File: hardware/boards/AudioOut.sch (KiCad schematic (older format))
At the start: 9 parts, among them J4 AudioJack3_SwitchTR

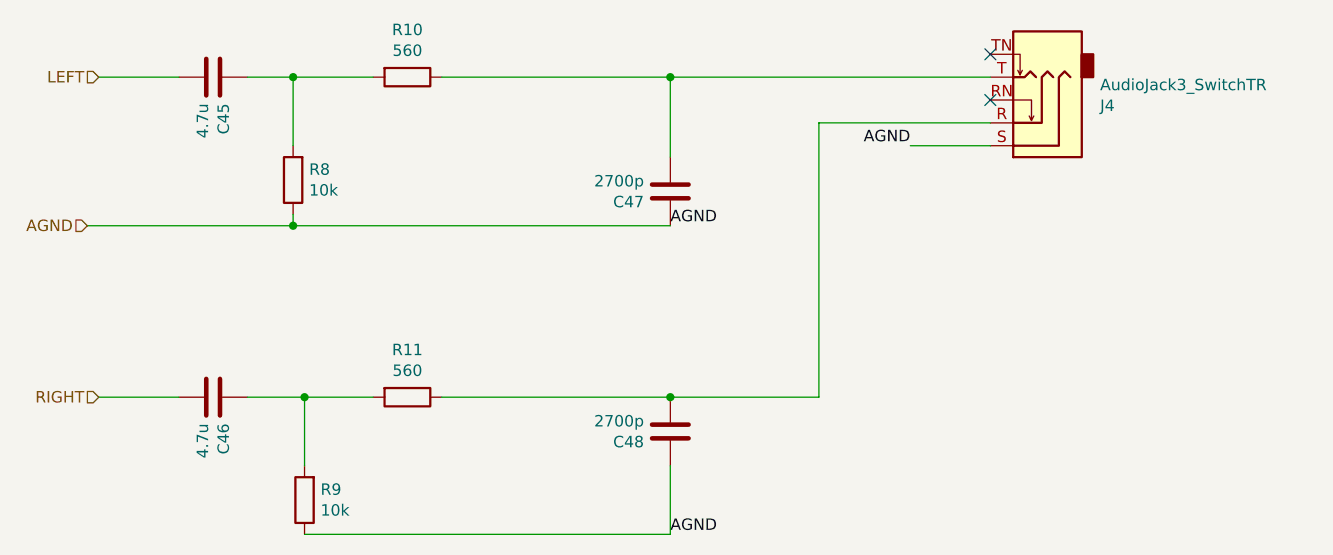
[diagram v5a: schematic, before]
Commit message: mainboard passes drc
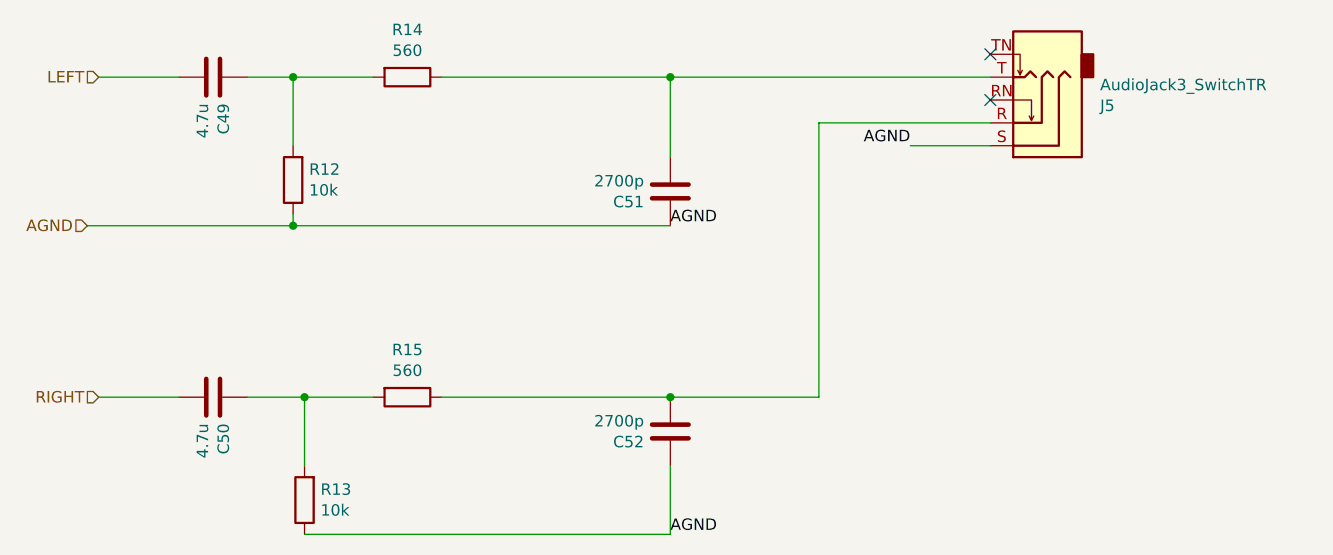
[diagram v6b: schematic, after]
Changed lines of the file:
@@
 $Descr A4 11693 8268
 encoding utf-8
-Sheet 2 8
+Sheet 3 8
 Title ""
 Date ""
@@
 AR Path="/5F0E4EB0/5F0C0CCE" Ref="C69"  Part="1"
 AR Path="/5F0EA26D/5F0C0CCE" Ref="C53"  Part="1"
-F 0 "C45" H 3115 2946 50  0000 L CNN
+F 0 "C49" H 3115 2946 50  0000 L CNN
 F 1 "4.7u" H 3115 2855 50  0000 L CNN
 F 2 "Capacitor_SMD:C_0805_2012Metric" H 3038 2750 50  0001 C CNN
@@
 AR Path="/5F0E4EB0/5F0C0D6D" Ref="C70"  Part="1"
 AR Path="/5F0EA26D/5F0C0D6D" Ref="C54"  Part="1"
-F 0 "C46" H 3115 4346 50  0000 L CNN
+F 0 "C50" H 3115 4346 50  0000 L CNN
 F 1 "4.7u" H 3115 4255 50  0000 L CNN
 F 2 "Capacitor_SMD:C_0805_2012Metric" H 3038 4150 50  0001 C CNN
@@
 AR Path="/5F0E4EB0/5F0C13C6" Ref="R34"  Part="1"
 AR Path="/5F0EA26D/5F0C13C6" Ref="R18"  Part="1"
-F 0 "R10" V 3643 2900 50  0000 C CNN
+F 0 "R14" V 3643 2900 50  0000 C CNN
 F 1 "560" V 3734 2900 50  0000 C CNN
 F 2 "Resistor_SMD:R_0805_2012Metric" V 3780 2900 50  0001 C CNN
@@
 AR Path="/5F0E4EB0/5F0C1FD3" Ref="R35"  Part="1"
 AR Path="/5F0EA26D/5F0C1FD3" Ref="R19"  Part="1"
-F 0 "R11" V 3643 4300 50  0000 C CNN
+F 0 "R15" V 3643 4300 50  0000 C CNN
 F 1 "560" V 3734 4300 50  0000 C CNN
 F 2 "Resistor_SMD:R_0805_2012Metric" V 3780 4300 50  0001 C CNN
@@
 AR Path="/5F0E4EB0/5F0C25D6" Ref="R33"  Part="1"
 AR Path="/5F0EA26D/5F0C25D6" Ref="R17"  Part="1"
-F 0 "R9" H 3330 4704 50  0000 R CNN
+F 0 "R13" H 3330 4704 50  0000 R CNN
 F 1 "10k" H 3330 4795 50  0000 R CNN
 F 2 "Resistor_SMD:R_0805_2012Metric" V 3330 4750 50  0001 C CNN
@@
 AR Path="/5F0E4EB0/5F0C364C" Ref="R32"  Part="1"
 AR Path="/5F0EA26D/5F0C364C" Ref="R16"  Part="1"
-F 0 "R8" H 3280 3304 50  0000 R CNN
+F 0 "R12" H 3280 3304 50  0000 R CNN
 F 1 "10k" H 3280 3395 50  0000 R CNN
 F 2 "Resistor_SMD:R_0805_2012Metric" V 3280 3350 50  0001 C CNN
@@
 AR Path="/5F0E4EB0/5F0C409A" Ref="C72"  Part="1"
 AR Path="/5F0EA26D/5F0C409A" Ref="C56"  Part="1"
-F 0 "C48" H 5115 4496 50  0000 L CNN
+F 0 "C52" H 5115 4496 50  0000 L CNN
 F 1 "2700p" H 5115 4405 50  0000 L CNN
 F 2 "Capacitor_SMD:C_0805_2012Metric" H 5038 4300 50  0001 C CNN
@@
 AR Path="/5F0E4EB0/5F0C470A" Ref="C71"  Part="1"
 AR Path="/5F0EA26D/5F0C470A" Ref="C55"  Part="1"
-F 0 "C47" H 5115 3446 50  0000 L CNN
+F 0 "C51" H 5115 3446 50  0000 L CNN
 F 1 "2700p" H 5115 3355 50  0000 L CNN
 F 2 "Capacitor_SMD:C_0805_2012Metric" H 5038 3250 50  0001 C CNN
@@
 AR Path="/5F0E4EB0/5F0C56B0" Ref="J10"  Part="1"
 AR Path="/5F0EA26D/5F0C56B0" Ref="J6"  Part="1"
-F 0 "J4" H 6320 3025 50  0000 R CNN
+F 0 "J5" H 6320 3025 50  0000 R CNN
 F 1 "AudioJack3_SwitchTR" H 6320 2934 50  0000 R CNN
 F 2 "footprints:ACJS-MV5" H 6600 3100 50  0001 C CNN

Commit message: Breakout: changed from 4 layer to 2 layer; Mainboard: add serial daisy chain RX/TX to RX4/TX4
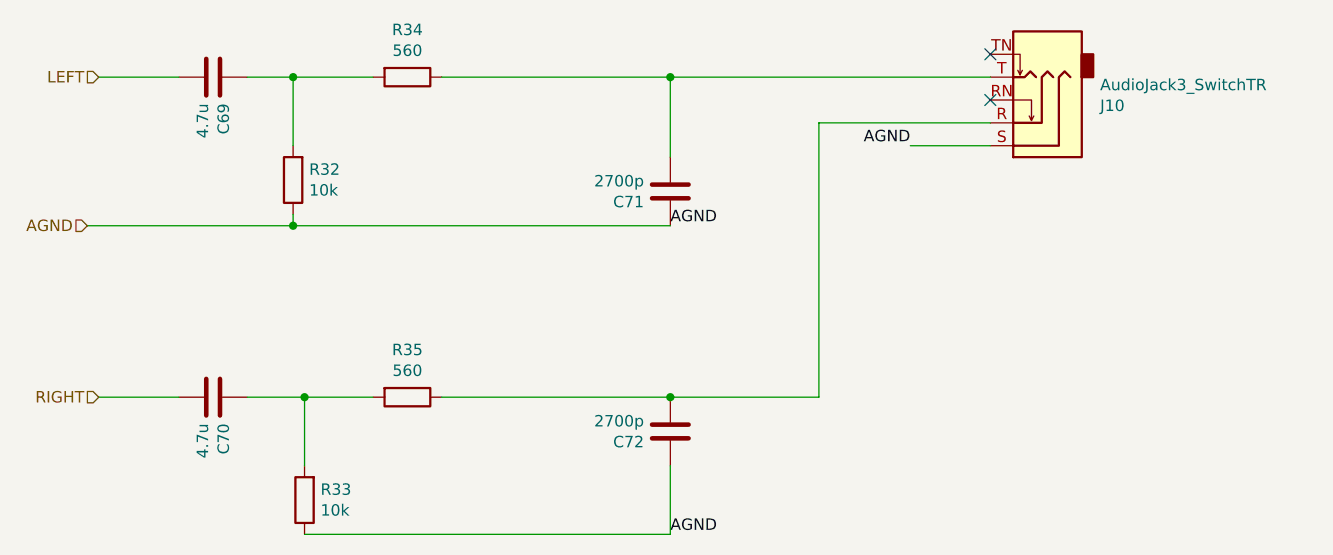
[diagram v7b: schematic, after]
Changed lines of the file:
@@
 AR Path="/5F0E4EB0/5F0C0CCE" Ref="C69"  Part="1"
 AR Path="/5F0EA26D/5F0C0CCE" Ref="C53"  Part="1"
-F 0 "C49" H 3115 2946 50  0000 L CNN
+F 0 "C69" H 3115 2946 50  0000 L CNN
 F 1 "4.7u" H 3115 2855 50  0000 L CNN
 F 2 "Capacitor_SMD:C_0805_2012Metric" H 3038 2750 50  0001 C CNN
@@
 AR Path="/5F0E4EB0/5F0C0D6D" Ref="C70"  Part="1"
 AR Path="/5F0EA26D/5F0C0D6D" Ref="C54"  Part="1"
-F 0 "C50" H 3115 4346 50  0000 L CNN
+F 0 "C70" H 3115 4346 50  0000 L CNN
 F 1 "4.7u" H 3115 4255 50  0000 L CNN
 F 2 "Capacitor_SMD:C_0805_2012Metric" H 3038 4150 50  0001 C CNN
@@
 AR Path="/5F0E4EB0/5F0C13C6" Ref="R34"  Part="1"
 AR Path="/5F0EA26D/5F0C13C6" Ref="R18"  Part="1"
-F 0 "R14" V 3643 2900 50  0000 C CNN
+F 0 "R34" V 3643 2900 50  0000 C CNN
 F 1 "560" V 3734 2900 50  0000 C CNN
 F 2 "Resistor_SMD:R_0805_2012Metric" V 3780 2900 50  0001 C CNN
@@
 AR Path="/5F0E4EB0/5F0C1FD3" Ref="R35"  Part="1"
 AR Path="/5F0EA26D/5F0C1FD3" Ref="R19"  Part="1"
-F 0 "R15" V 3643 4300 50  0000 C CNN
+F 0 "R35" V 3643 4300 50  0000 C CNN
 F 1 "560" V 3734 4300 50  0000 C CNN
 F 2 "Resistor_SMD:R_0805_2012Metric" V 3780 4300 50  0001 C CNN
@@
 AR Path="/5F0E4EB0/5F0C25D6" Ref="R33"  Part="1"
 AR Path="/5F0EA26D/5F0C25D6" Ref="R17"  Part="1"
-F 0 "R13" H 3330 4704 50  0000 R CNN
+F 0 "R33" H 3330 4704 50  0000 R CNN
 F 1 "10k" H 3330 4795 50  0000 R CNN
 F 2 "Resistor_SMD:R_0805_2012Metric" V 3330 4750 50  0001 C CNN
@@
 AR Path="/5F0E4EB0/5F0C364C" Ref="R32"  Part="1"
 AR Path="/5F0EA26D/5F0C364C" Ref="R16"  Part="1"
-F 0 "R12" H 3280 3304 50  0000 R CNN
+F 0 "R32" H 3280 3304 50  0000 R CNN
 F 1 "10k" H 3280 3395 50  0000 R CNN
 F 2 "Resistor_SMD:R_0805_2012Metric" V 3280 3350 50  0001 C CNN
@@
 AR Path="/5F0E4EB0/5F0C409A" Ref="C72"  Part="1"
 AR Path="/5F0EA26D/5F0C409A" Ref="C56"  Part="1"
-F 0 "C52" H 5115 4496 50  0000 L CNN
+F 0 "C72" H 5115 4496 50  0000 L CNN
 F 1 "2700p" H 5115 4405 50  0000 L CNN
 F 2 "Capacitor_SMD:C_0805_2012Metric" H 5038 4300 50  0001 C CNN
@@
 AR Path="/5F0E4EB0/5F0C470A" Ref="C71"  Part="1"
 AR Path="/5F0EA26D/5F0C470A" Ref="C55"  Part="1"
-F 0 "C51" H 5115 3446 50  0000 L CNN
+F 0 "C71" H 5115 3446 50  0000 L CNN
 F 1 "2700p" H 5115 3355 50  0000 L CNN
 F 2 "Capacitor_SMD:C_0805_2012Metric" H 5038 3250 50  0001 C CNN
@@
 AR Path="/5F0E4EB0/5F0C56B0" Ref="J10"  Part="1"
 AR Path="/5F0EA26D/5F0C56B0" Ref="J6"  Part="1"
-F 0 "J5" H 6320 3025 50  0000 R CNN
+F 0 "J10" H 6320 3025 50  0000 R CNN
 F 1 "AudioJack3_SwitchTR" H 6320 2934 50  0000 R CNN
 F 2 "footprints:ACJS-MV5" H 6600 3100 50  0001 C CNN
